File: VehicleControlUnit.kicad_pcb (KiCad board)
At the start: 2 copper layers, 86.6 x 93.8 mm, 101 parts, among them Con1 LED, Con2 LED, J1 Conn_01x02, J10 Conn_01x04, J11 Conn_01x04, J12 SFH11-PBPC-D05-ST-BK, J13 SFH11-PBPC-D05-ST-BK, J2 Conn_01x02, J3 Conn_01x02, J5 SFH11-PBPC-D05-ST-BK, J6 Conn_01x04, J7 Conn_01x04, J8 Conn_01x04, J9 USB_C_Receptacle_USB2.0_16P, Q1 PSMN8R5-40MSDX, Q2 IRLML0030, Q3 IRLML0030, SW1 RESET, SW2 BOOT, U1 LM74501-Q1, U2 TLV1117LV33DCYR, U4 ESP32-C6-MINI-1/U, U5 TCMT1106, U6 TCMT1106

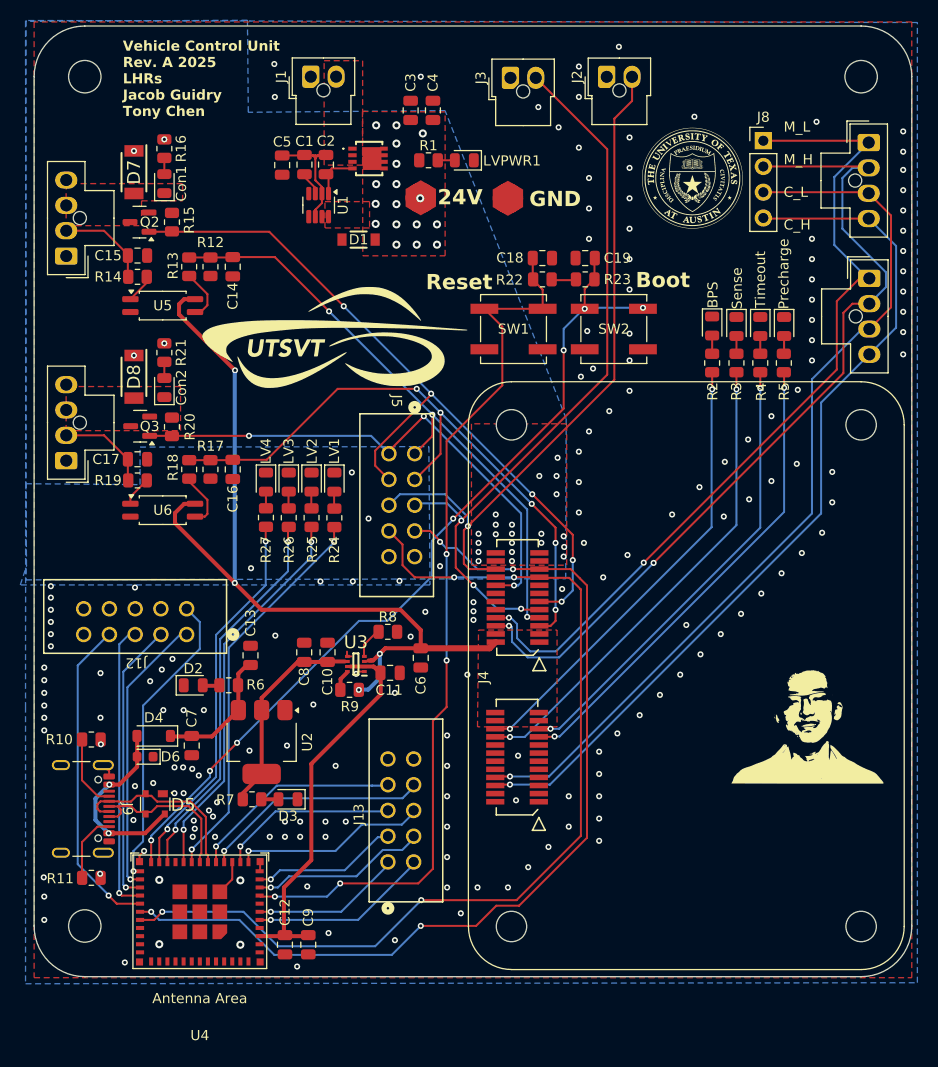
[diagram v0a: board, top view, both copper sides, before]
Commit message: replaced 0805 with 0603, changed logic analyzer symbol and silkscreen
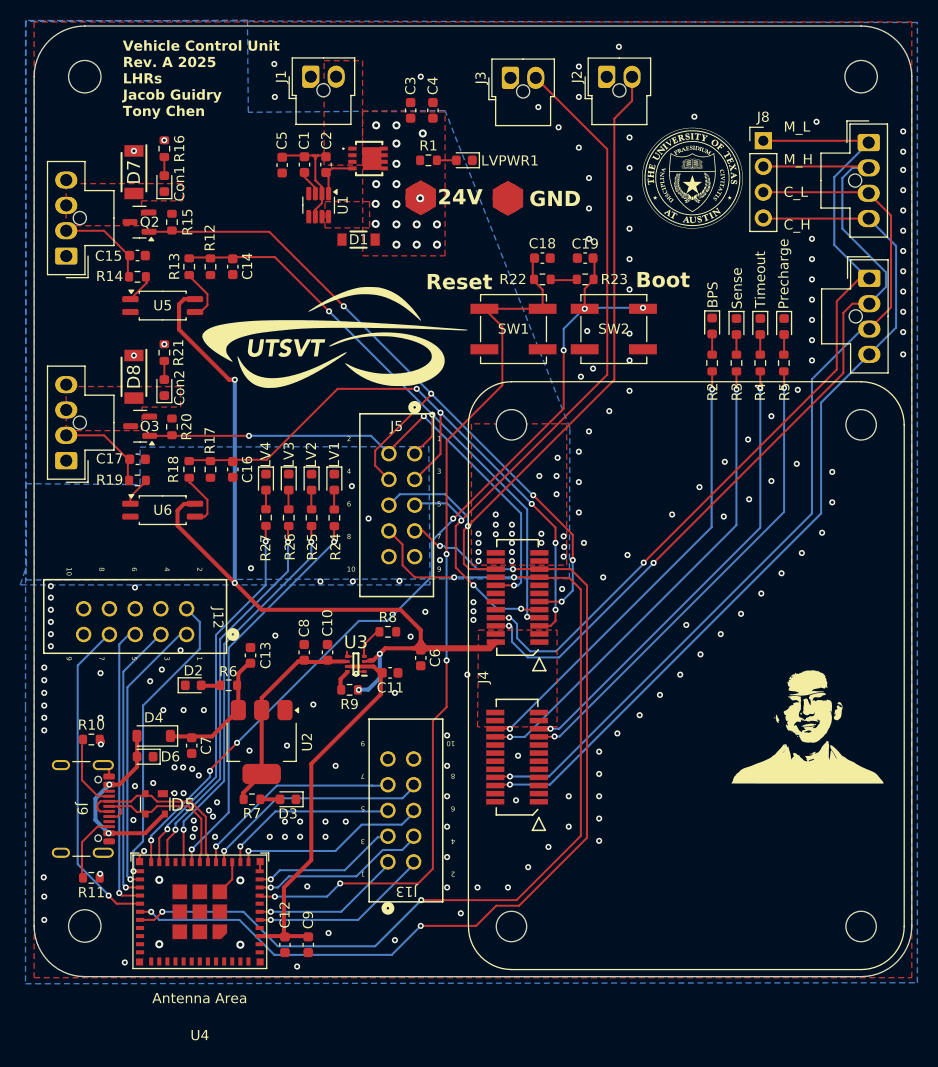
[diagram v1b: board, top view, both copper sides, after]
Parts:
- added G***: LOGO, UTSVT_Logos:Hallock_Image_Tiny, B.Cu at (185.6, 117.2)
- C1, C10, C11, C12, C13, C14, C15, C16, C17, C18, C19, C2, C3, C4, C5, C6, C7, C8, C9: footprint Capacitor_SMD:C_0805_2012Metric -> Capacitor_SMD:C_0603_1608Metric
- Con1, Con2, D2, D3, LED1, LED2, LED3, LED4, LV1, LV2, LV3, LV4, LVPWR1: footprint LED_SMD:LED_0805_2012Metric -> LED_SMD:LED_0603_1608Metric
- R1, R10, R11, R12, R13, R14, R15, R16, R17, R18, R19, R2, R20, R21, R22, R23, R24, R25, R26, R27, R3, R4, R5, R6, R7, R8, R9: footprint Resistor_SMD:R_0805_2012Metric -> Resistor_SMD:R_0603_1608Metric
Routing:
- net 3V3_LSOM: track 85.3 -> 87.2 mm
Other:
- board text added: "1 3 5 7 9"
- board text added: "2 4 6 8 10"
